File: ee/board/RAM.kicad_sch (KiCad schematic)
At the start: 40 parts, among them U3 MT41K256M16TW-107_P

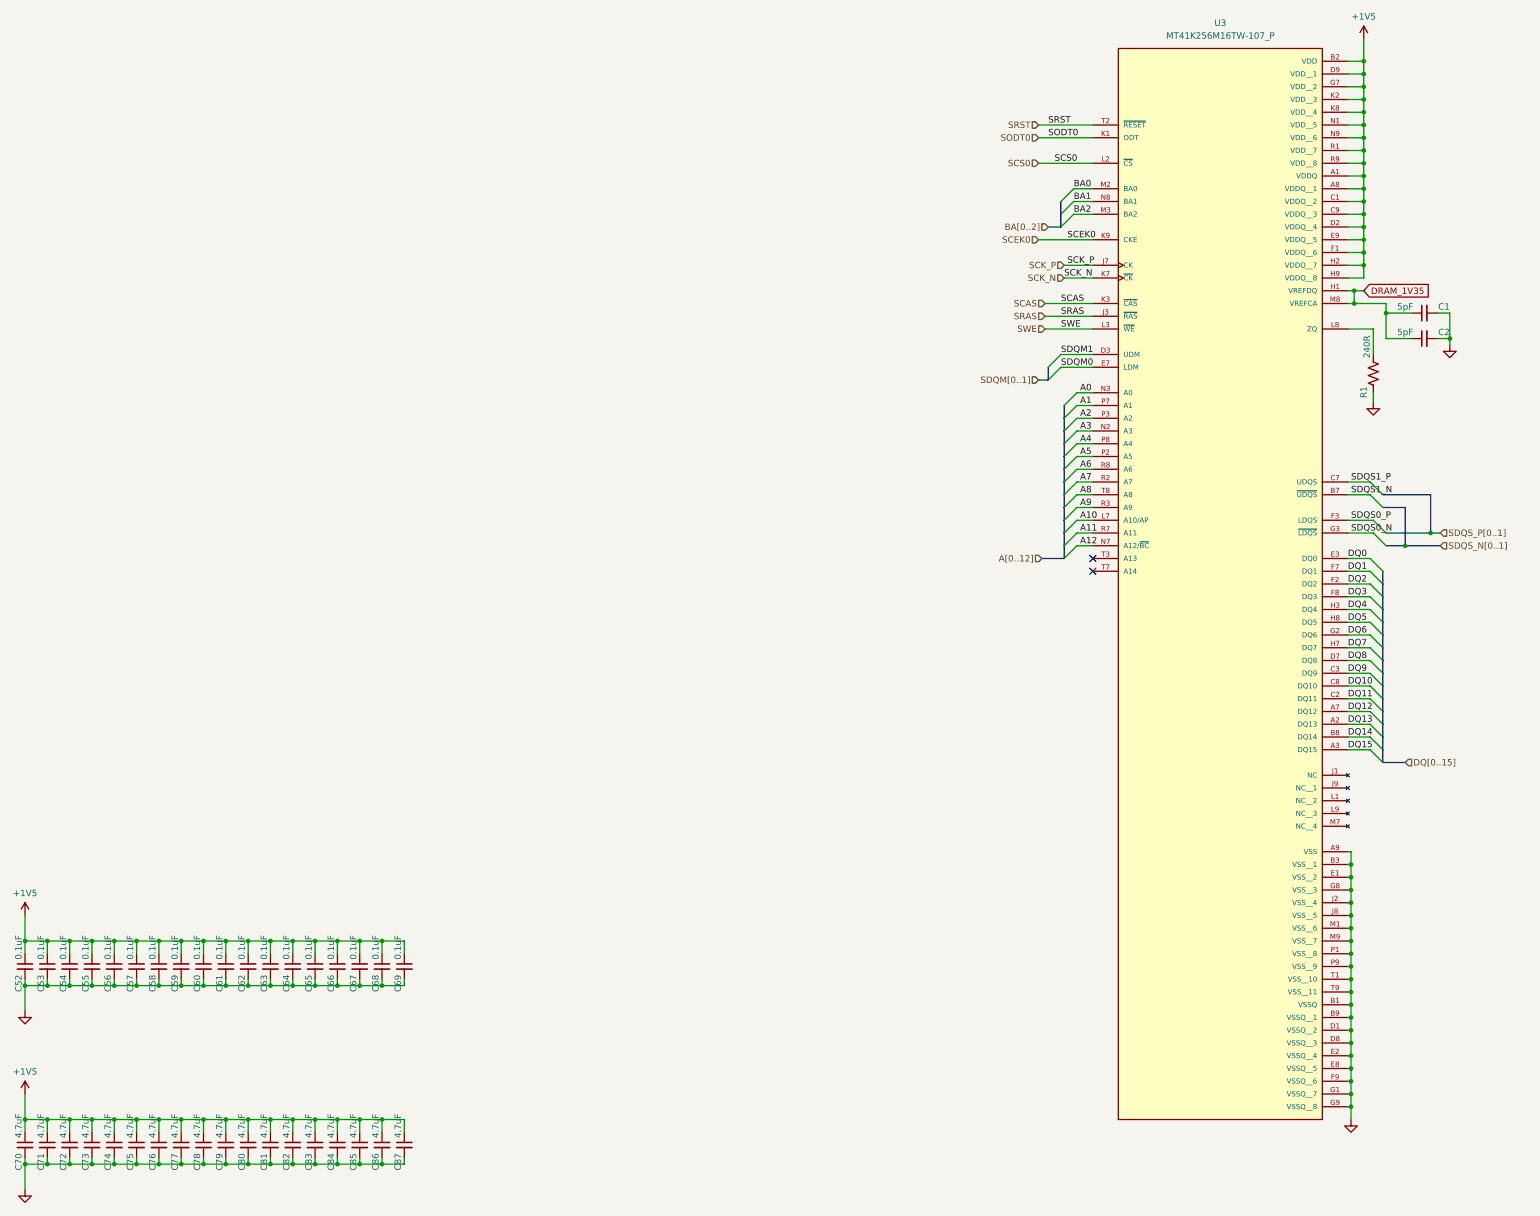
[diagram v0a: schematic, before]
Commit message: Added the footprints into the design.
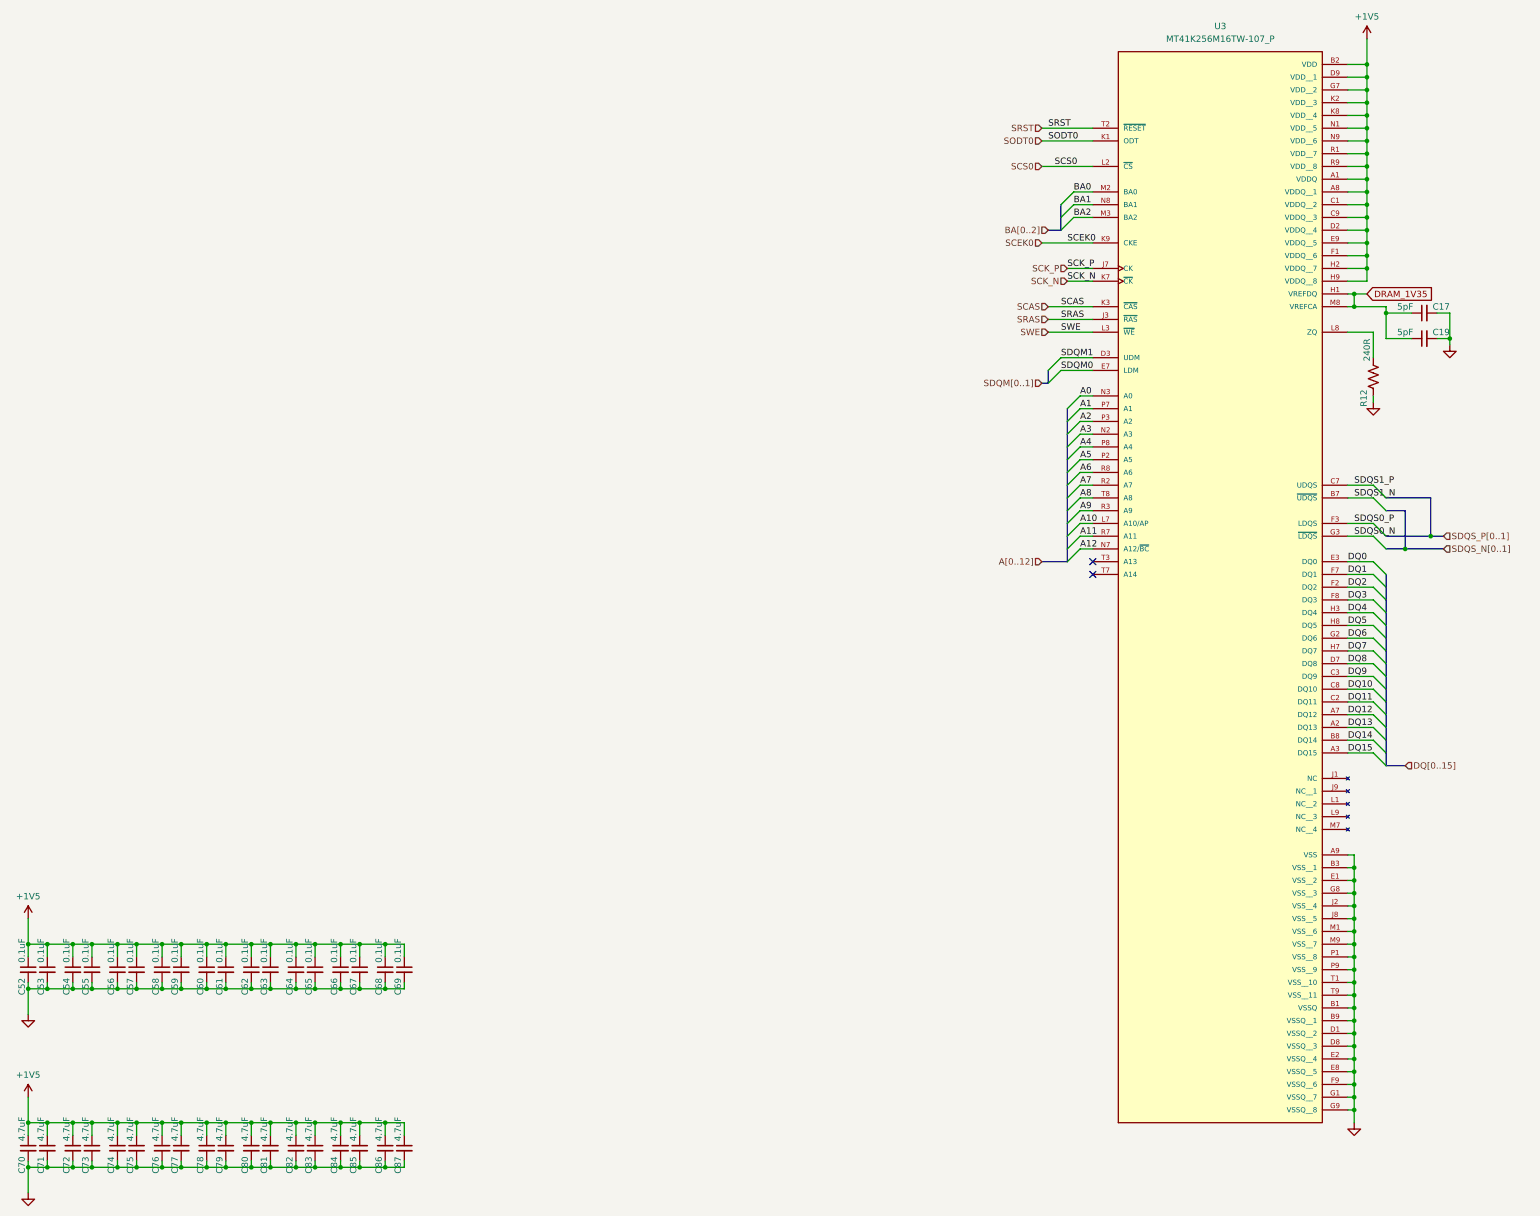
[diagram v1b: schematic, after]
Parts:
- U3: footprint MT41K256M16TW_107_P:BGA96C80P9X16_1400X800X120 -> ddr3:BGA96C80P9X16_1400X800X120
- renumbered C1 to C17, C2 to C19, R1 to R12
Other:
- moved on the sheet: C52, C53, C54, C55, C56, C57, C58, C59, C60, C61, C62, C63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
